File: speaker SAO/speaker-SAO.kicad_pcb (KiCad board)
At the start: 2 copper layers, 78.8 x 16.5 mm, 3 parts

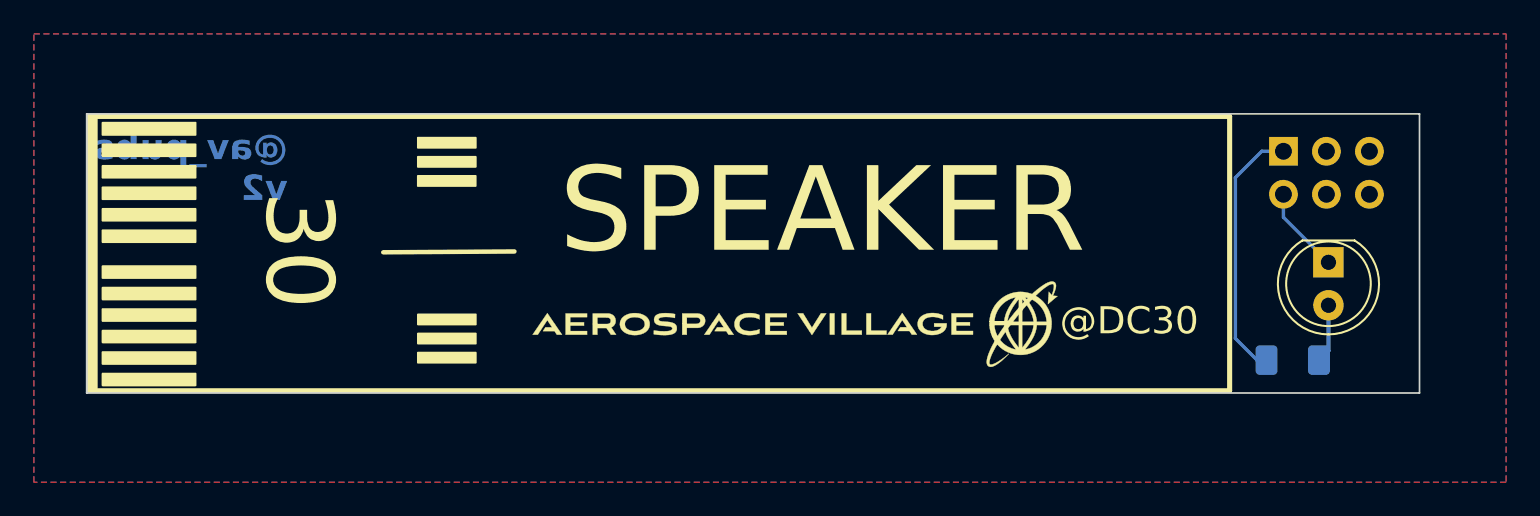
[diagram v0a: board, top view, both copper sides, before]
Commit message: speaker and crew SAOs updated to v3 that moves the connector slightly so it doesn't stick out
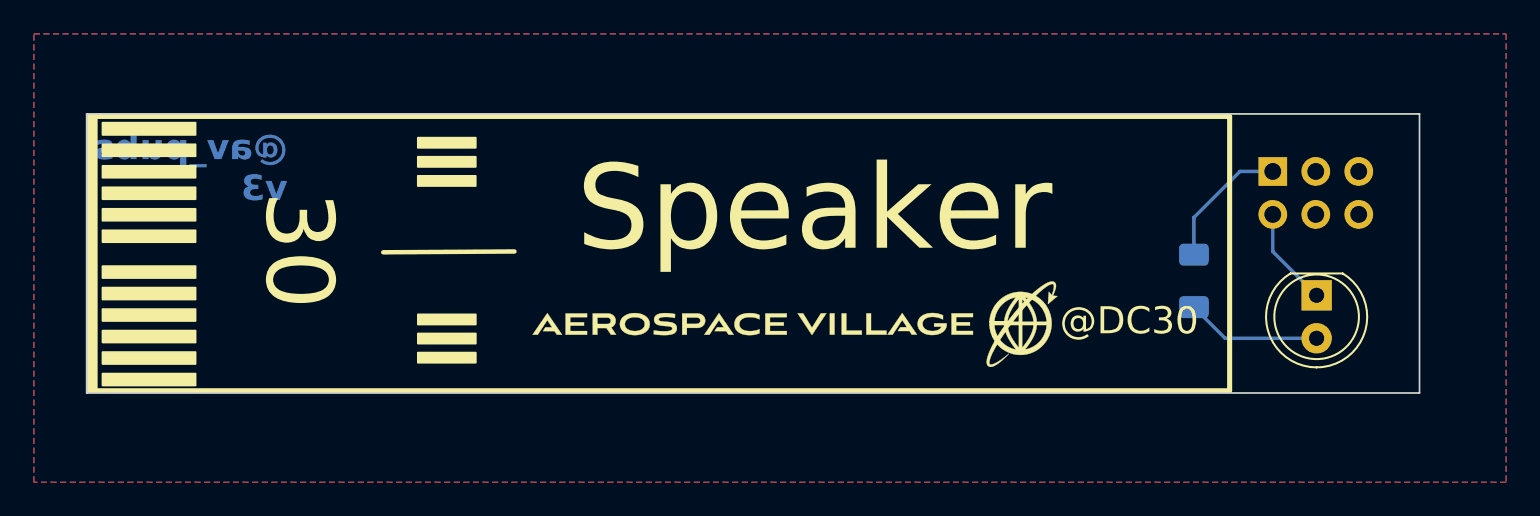
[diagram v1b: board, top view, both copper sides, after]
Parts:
- moved REF** 7.48 mm to (149.6, 132.6), turned to -90 degrees
- moved REF** 2.07 mm to (156.8, 133.4)
- moved REF** 1.35 mm to (154.2, 126.1)
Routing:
- net (no net): track 24.0 -> 21.9 mm
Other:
- board text added: "@av_pubs v3"
- board text added: "Speaker"
- board text removed: "@av_pubs v2"
- board text removed: "SPEAKER"
